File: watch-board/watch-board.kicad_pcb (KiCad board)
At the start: 2 copper layers, 39.2 x 40 mm, 44 parts, among them J1 Conn_01x05_Male, J2 Conn_02x05, J3 FPC-Conn_01x08, U1 MCU_STM32L051K8Tx, U2 Regulator_LTC3531-3, U3 Regulator_BQ25504

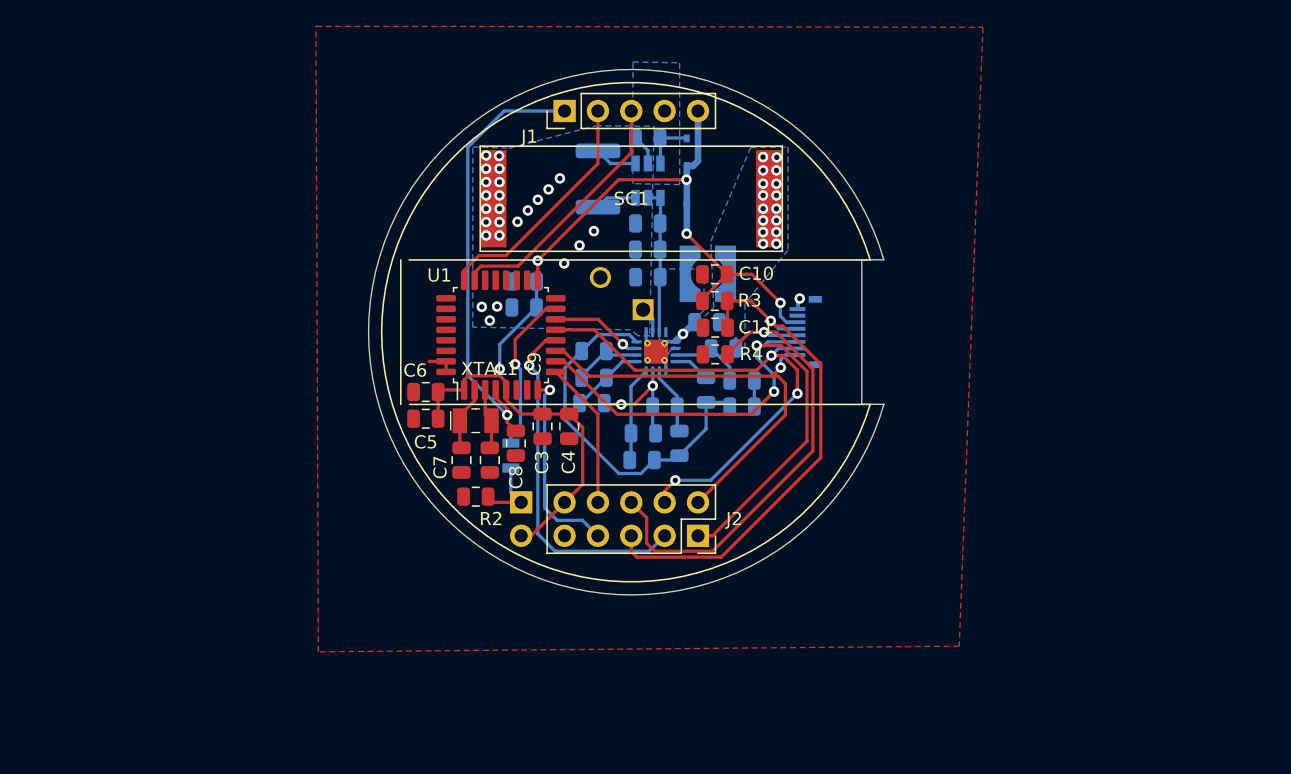
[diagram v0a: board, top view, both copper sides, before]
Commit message: Stopping work on Watch-V2. Changing driver & Display on Watch-V1.
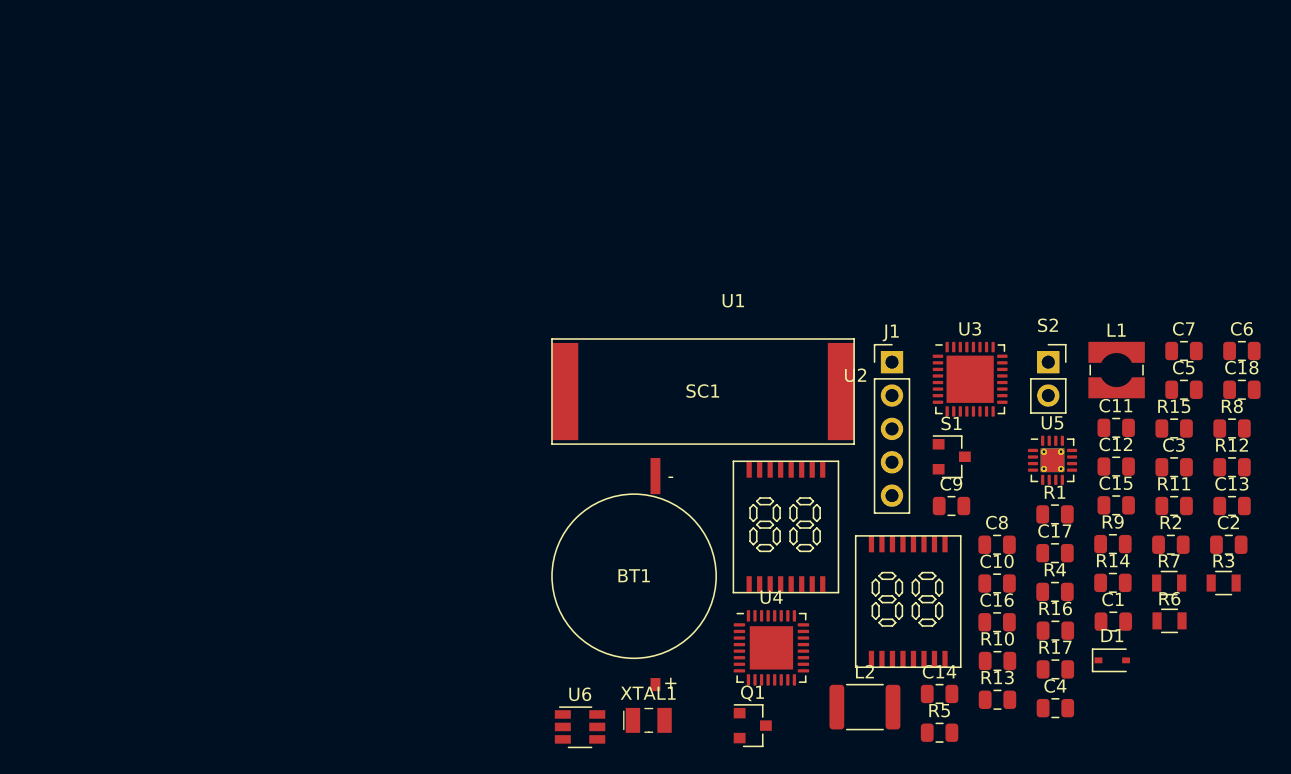
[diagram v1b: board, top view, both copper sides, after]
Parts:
- removed J2: Conn_02x05, Connector_PinSocket_2.54mm:PinSocket_2x05_P2.54mm_Vertical
- removed J3: FPC-Conn_01x08, luke-footprints:Connector_Molex-5014610891
- added C18: C_0.1uF, Capacitor_SMD:C_0805_2012Metric, F.Cu at (186.5, 104.4)
- added Q1: Transistor_MMBT3906, Package_TO_SOT_SMD:SOT-23, F.Cu at (149.2, 130.0)
- added R15: R_6.04M, Resistor_SMD:R_0805_2012Metric, F.Cu at (181.3, 107.3)
- added R16: R_10M, Resistor_SMD:R_0805_2012Metric, F.Cu at (172.3, 122.7)
- added R17: R_3.83M, Resistor_SMD:R_0805_2012Metric, F.Cu at (172.3, 125.7)
- added S2: Switch_1767, Connector_PinSocket_2.54mm:PinSocket_1x02_P2.54mm_Vertical, F.Cu at (171.7, 102.3)
- added U4: MCU_STM32L051K8Ux, Package_DFN_QFN:QFN-32-1EP_5x5mm_P0.5mm_EP3.3x3.3mm, F.Cu at (150.7, 124.0)
- added U5: Regulator_BQ25504, Package_DFN_QFN:VQFN-16-1EP_3x3mm_P0.5mm_EP1.8x1.8mm_ThermalVias, F.Cu at (172.1, 109.8)
- added U6: Regulator_LTC3531-3, Package_TO_SOT_SMD:TSOT-23-6, F.Cu at (136.1, 130.1)
- BT1: footprint Battery:Battery_Panasonic_CR1220-VCN_Vertical_CircularHoles -> luke-footprints:BAT_ML1220-F1A; moved to F.Cu
- C1, C13, C14, C2, D1, R10: moved to F.Cu
- C10: value C_2.2uF -> C_0.1uF
- C12: value C_2.2uF -> C_1uF; moved to F.Cu
- C15: value C_10uF -> C_2.2uF; moved to F.Cu
- C16: value C_4.7uF -> C_10uF; moved to F.Cu
- C17: value C_0.1uF -> C_4.7uF; moved to F.Cu
- L1: value L_10uH -> L_22uH; footprint Inductor_SMD:L_1812_4532Metric -> Inductor_SMD:L_Wuerth_WE-TPC-3816; moved to F.Cu
- L2: value L_22uH -> L_10uH; footprint Inductor_SMD:L_Wuerth_WE-TPC-3816 -> Inductor_SMD:L_1812_4532Metric; moved to F.Cu
- R1: value R_330 -> R_1K; footprint footprints:R_0805_OEM -> Resistor_SMD:R_0805_2012Metric; moved to F.Cu
- R11: value R_5.11M -> R_5.62M; moved to F.Cu
- R12: value R_6.04M -> R_806K; moved to F.Cu
- R13: value R_10M -> R_4.22M; moved to F.Cu
- R14: value R_3.83M -> R_5.11M; moved to F.Cu
- R2: value R_220K -> R_1K
- R3: value R_10K -> R_330; footprint Resistor_SMD:R_0805_2012Metric -> footprints:R_0805_OEM
- R4: value R_10K -> R_220K
- R5: value R_3.74M -> R_1K; moved to F.Cu
- R6: value R_6.19M -> R_330; footprint Resistor_SMD:R_0805_2012Metric -> footprints:R_0805_OEM; moved to F.Cu
- R7: value R_4.22M -> R_330; footprint Resistor_SMD:R_0805_2012Metric -> footprints:R_0805_OEM; moved to F.Cu
- R8: value R_5.62M -> R_3.74M; moved to F.Cu
- R9: value R_806K -> R_6.19M; moved to F.Cu
- S1: value Switch_1767 -> Switch_RR121-1A23-311; footprint Connector_PinSocket_2.54mm:PinSocket_1x02_P2.54mm_Vertical -> Package_TO_SOT_SMD:SOT-23; moved to F.Cu
- U1: value MCU_STM32L051K8Tx -> LCD_OD-204; footprint Package_QFP:LQFP-32_7x7mm_P0.8mm -> luke-footprints:LCD_OD-204
- U2: value Regulator_LTC3531-3 -> LCD_OD-204; footprint Package_TO_SOT_SMD:TSOT-23-6 -> luke-footprints:LCD_OD-204; moved to F.Cu
- U3: value Regulator_BQ25504 -> Display-Driver_PCA8561ANH; footprint Package_DFN_QFN:VQFN-16-1EP_3x3mm_P0.5mm_EP1.8x1.8mm_ThermalVias -> Package_DFN_QFN:QFN-32-1EP_5x5mm_P0.5mm_EP3.6x3.6mm; moved to F.Cu
- moved C6 62.2 mm to (186.5, 101.4)
- moved C5 57.8 mm to (182.1, 104.4)
- moved C2 57.3 mm to (185.5, 116.2)
- moved C7 55.6 mm to (182.1, 101.4), turned to 0 degrees
- moved R2 53.0 mm to (181.1, 116.2), turned to 0 degrees
- moved C1 50.8 mm to (176.7, 122.0)
- moved D1 50.5 mm to (176.6, 125.0), turned to 0 degrees
- moved C3 48.2 mm to (181.3, 110.3), turned to 0 degrees
- moved R11 45.7 mm to (181.3, 113.2), turned to 0 degrees
- moved C15 45.3 mm to (176.9, 113.2), turned to 0 degrees
- moved R8 45.0 mm to (185.7, 107.3)
- moved R3 44.3 mm to (185.1, 119.1)
- moved C4 42.8 mm to (172.3, 128.6), turned to 0 degrees
- moved L1 42.1 mm to (176.9, 102.9), turned to 0 degrees
- moved R1 41.7 mm to (172.3, 113.9), turned to 0 degrees
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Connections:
- C10 pad 1: VDD -> /VDISP
- C10 pad 2: GND -> Net-(C10-Pad2)
- C11 pad 1: /DISP -> /VDISP
- C11 pad 2: GND -> Net-(C11-Pad2)
- C12 pad 1: /LOAD -> VDD
- C15 pad 1: Net-(C15-Pad1) -> /LOAD
- C16 pad 1: /LOAD -> Net-(C16-Pad1)
- D1 pad 2: Net-(C15-Pad1) -> Net-(C16-Pad1)
- L1 pad 1: Net-(L1-Pad1) -> Net-(C14-Pad1)
- L2 pad 1: Net-(C14-Pad1) -> Net-(L2-Pad1)
- R1 pad 1: Net-(R1-Pad1) -> VCC
- R1 pad 2: /BUTTON -> /SDA
- R10 pad 1: /OK_HYST -> Net-(R10-Pad1)
- R10 pad 2: /OK_PROG -> /VBAT_UV
- R11 pad 1: /OK_PROG -> /VBAT_UV
- R12 pad 1: Net-(R12-Pad1) -> Net-(R10-Pad1)
- R12 pad 2: GND -> /OK_HYST
- R13 pad 1: Net-(R13-Pad1) -> /OK_HYST
- R13 pad 2: Net-(R12-Pad1) -> /OK_PROG
- R14 pad 1: Net-(C14-Pad1) -> /OK_PROG
- R14 pad 2: Net-(R13-Pad1) -> GND
- R2 pad 1: Net-(R1-Pad1) -> VCC
- R2 pad 2: GND -> /SCL
- R3 pad 1: VDD -> Net-(R3-Pad1)
- R3 pad 2: /DISP -> /BUTTON
- R4 pad 1: /EXTCOMIN -> Net-(R3-Pad1)
- R5 pad 1: Net-(R5-Pad1) -> VCC
- R5 pad 2: /VBAT_OV -> Net-(Q1-Pad1)
- R6 pad 1: /VBAT_OV -> Net-(R6-Pad1)
- R6 pad 2: GND -> /SWITCH
- R7 pad 1: Net-(R5-Pad1) -> Net-(Q1-Pad1)
- R7 pad 2: /VBAT_UV -> /DISP
- R8 pad 1: /VBAT_UV -> Net-(R10-Pad1)
- R8 pad 2: GND -> /VBAT_OV
- R9 pad 1: Net-(R5-Pad1) -> /VBAT_OV
- R9 pad 2: /OK_HYST -> GND
- S1 pad 1: Net-(R1-Pad1) -> VDD
- S1 pad 2: VDD -> Net-(R6-Pad1)
- U1 pad 1: VDD -> /COM1
- U1 pad 10: /NSS -> /2A
- U1 pad 11: /SCK -> /2B
- U1 pad 12: /MISO -> /2C
- U1 pad 13: /MOSI -> /2D
- U1 pad 14: /VBAT_OK -> /2E
- U1 pad 15: /BUTTON -> /2F
- U1 pad 16: GND -> /2G
- U1 pad 2: Net-(C7-Pad1) -> /1G
- U1 pad 3: Net-(C9-Pad1) -> /1F
- U1 pad 4: /RST -> /1E
- U1 pad 5: VDD -> /1D
- U1 pad 6: Net-(U1-Pad6) -> /1C
- U1 pad 7: Net-(U1-Pad7) -> /1B
- U1 pad 8: /PA2 -> /1A
- U1 pad 9: /PA3 -> Net-(U1-Pad9)
- U2 pad 1: Net-(L1-Pad2) -> /COM2
- U2 pad 2: GND -> /1G
- U2 pad 3: Net-(C15-Pad1) -> /1F
- U2 pad 4: /LOAD -> /1E
- U2 pad 5: /LOAD -> /1D
- U2 pad 6: Net-(L1-Pad1) -> /1C
- U3 pad 1: GND -> /COM2
- U3 pad 10: /OK_PROG -> GND
- U3 pad 11: /VBAT_OK -> GND
- U3 pad 12: GND -> /1G
- U3 pad 13: GND -> /1F
- U3 pad 14: Net-(BT1-Pad1) -> /1E
- U3 pad 15: /LOAD -> /1D
- U3 pad 16: Net-(L2-Pad2) -> /1C
- U3 pad 17: GND -> /1B
- U3 pad 2: Net-(C14-Pad1) -> Net-(C11-Pad2)
- U3 pad 3: Net-(R13-Pad1) -> Net-(C10-Pad2)
- U3 pad 4: Net-(C13-Pad1) -> GND
- U3 pad 5: GND -> /RESET
- U3 pad 6: /VBAT_OV -> GND
- U3 pad 7: Net-(R5-Pad1) -> Net-(U3-Pad7)
- U3 pad 8: /VBAT_UV -> /SCL
- U3 pad 9: /OK_HYST -> /SDA
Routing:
- net VDD: track 76.8 -> 0.00 mm, vias 5 -> 0
- net /NSS: track 46.9 -> 0.00 mm, vias 2 -> 0
- net GND: track 41.6 -> 0.00 mm, vias 27 -> 0
- net /DISP: track 39.2 -> 0.00 mm, vias 1 -> 0
- net /MOSI: track 38.0 -> 0.00 mm, vias 3 -> 0
- net /EXTCOMIN: track 36.4 -> 0.00 mm, vias 1 -> 0
- net /RST: track 34.5 -> 0.00 mm, vias 1 -> 0
- net /SCK: track 32.7 -> 0.00 mm, vias 1 -> 0
- net /MISO: track 27.0 -> 0.00 mm, vias 1 -> 0
- net /SWDIO: track 19.5 -> 0.00 mm
- net /SWCLK: track 18.8 -> 0.00 mm
- net /PA2: track 15.0 -> 0.00 mm, vias 1 -> 0
- net /BUTTON: track 12.4 -> 0.00 mm, vias 1 -> 0
- net /LOAD: track 11.3 -> 0.00 mm
- net /PA3: track 11.3 -> 0.00 mm
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- removed copper zone on B.Cu, net GND
- removed copper zone on F.Cu, net GND
- removed copper zone on B.Cu, net Net-(C14-Pad1)
- removed copper zone on B.Cu, net Net-(L2-Pad2)
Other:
- board outline removed

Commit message: Starting Layout -- updated parts with smaller footprints for better layout
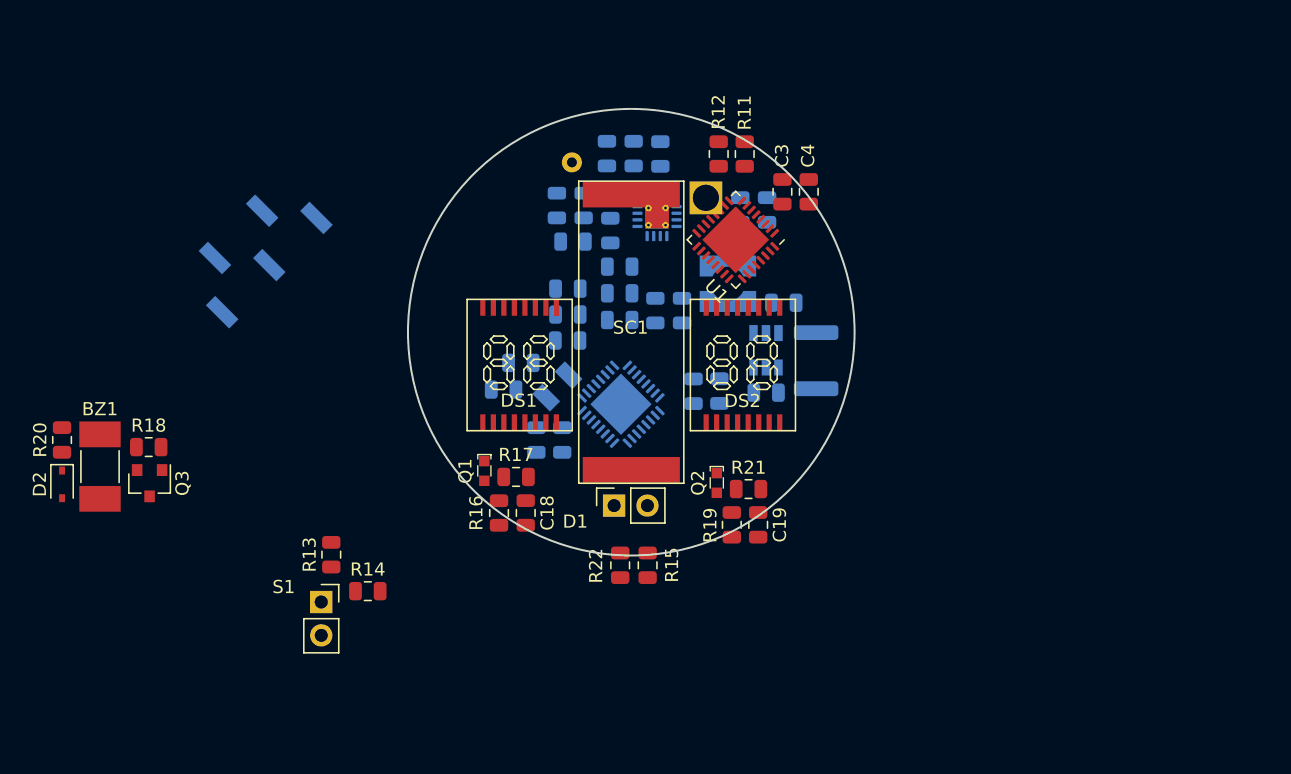
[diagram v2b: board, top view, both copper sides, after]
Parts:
- removed S2: Switch_1767, Connector_PinSocket_2.54mm:PinSocket_1x02_P2.54mm_Vertical
- removed U5: Regulator_BQ25504, Package_DFN_QFN:VQFN-16-1EP_3x3mm_P0.5mm_EP1.8x1.8mm_ThermalVias
- removed U6: Regulator_LTC3531-3, Package_TO_SOT_SMD:TSOT-23-6
- added BZ1: Buzzer_Piezo-35mm, Fuse:Fuse_Littelfuse-NANO2-451_453, F.Cu at (99.6, 110.2)
- added C19: C_100uF, Capacitor_SMD:C_0805_2012Metric, F.Cu at (149.7, 114.7)
- added D2: D-Schotkey_BAT54HT1G, Diode_SMD:D_SOD-323, F.Cu at (96.7, 111.6)
- added DS1: LCD_OD-204, luke-footprints:LCD_OD-204, F.Cu at (127.5, 97.5)
- added DS2: LCD_OD-204, luke-footprints:LCD_OD-204, F.Cu at (144.5, 97.5)
- added Q2: Phototransistor_ALS-PT19-315C, Digikey-footprints:LED_2-SMD_No_Lead_1.7x0.8mm, F.Cu at (146.5, 111.5)
- added Q3: Transistor_MMBT3904-TP, Package_TO_SOT_SMD:SOT-23, F.Cu at (103.3, 111.5)
- added R18: R_10K, Resistor_SMD:R_0805_2012Metric, F.Cu at (103.3, 108.7)
- added R19: R_4.87K, Resistor_SMD:R_0805_2012Metric, F.Cu at (147.7, 114.7)
- added R20: R_160, Resistor_SMD:R_0805_2012Metric, F.Cu at (96.7, 108.2)
- added R21: R_160, Resistor_SMD:R_0805_2012Metric, F.Cu at (148.9, 111.9)
- added R22: R_2.3K, Resistor_SMD:R_0805_2012Metric, F.Cu at (139.2, 117.7)
- BT1: value BAT_ML1220 -> BAT_ML2020-V1A; footprint luke-footprints:BAT_ML1220-F1A -> luke-footprints:Battery_Panasonic-ML-2020-V1A; moved to B.Cu
- C1: value C_0.1uF -> C_0.01uF; moved to B.Cu
- C10, C8, L1, L2, U4, XTAL1: moved to B.Cu
- C11: value C_0.1uF -> C_1uF; moved to B.Cu
- C12: value C_1uF -> C_0.1uF; moved to B.Cu
- C13: value C_0.01uF -> C_10uF; moved to B.Cu
- C14, C17: value C_4.7uF -> C_20pF; moved to B.Cu
- C15: value C_2.2uF -> C_10uF; moved to B.Cu
- C16, C6: value C_10uF -> C_0.1uF; moved to B.Cu
- C18: value C_0.1uF -> C_100uF
- C2: value C_1uF -> C_4.7uF; moved to B.Cu
- C4: value C_1uF -> C_0.1uF
- C5: value C_0.1uF -> C_4.7uF; moved to B.Cu
- C7: value C_20pF -> C_2.2uF; moved to B.Cu
- C9: value C_20pF -> C_1uF; moved to B.Cu
- D1: value D-Schotkey_BAT54HT1G -> LED_WP710A10LSECK-J4; footprint Diode_SMD:D_SOD-323 -> Connector_PinSocket_2.54mm:PinSocket_1x02_P2.54mm_Vertical
- J1: value Conn_01x05_Male -> Conn_01x05_Male_SMD; footprint Connector_PinHeader_2.54mm:PinHeader_1x05_P2.54mm_Vertical -> Connector_PinHeader_2.54mm:PinHeader_1x05_P2.54mm_Vertical_SMD_Pin1Left; moved to B.Cu
- Q1: value Transistor_MMBT3906 -> Phototransistor_ALS-PT19-315C; footprint Package_TO_SOT_SMD:SOT-23 -> Digikey-footprints:LED_2-SMD_No_Lead_1.7x0.8mm
- R1: value R_1K -> R_3.74M; moved to B.Cu
- R10: value R_4.22M -> R_3.83M; moved to B.Cu
- R11: value R_5.62M -> R_4.7K
- R12: value R_806K -> R_4.7K
- R13: value R_4.22M -> R_604
- R14: value R_5.11M -> R_10K
- R15: value R_6.04M -> R_1.5K
- R16: value R_10M -> R_4.87K
- R17: value R_3.83M -> R_160
- R2: value R_1K -> R_6.19M; moved to B.Cu
- R3, R6: value R_330 -> R_4.22M; footprint footprints:R_0805_OEM -> Resistor_SMD:R_0805_2012Metric; moved to B.Cu
- R4: value R_220K -> R_5.62M; moved to B.Cu
- R5: value R_1K -> R_806K; moved to B.Cu
- R7: value R_330 -> R_5.11M; footprint footprints:R_0805_OEM -> Resistor_SMD:R_0805_2012Metric; moved to B.Cu
- R8: value R_3.74M -> R_6.04M; moved to B.Cu
- R9: value R_6.19M -> R_10M; moved to B.Cu
- S1: value Switch_RR121-1A23-311 -> Switch_1767; footprint Package_TO_SOT_SMD:SOT-23 -> Connector_PinSocket_2.54mm:PinSocket_1x02_P2.54mm_Vertical
- U1: value LCD_OD-204 -> Display-Driver_PCA8561ANH; footprint luke-footprints:LCD_OD-204 -> Package_DFN_QFN:QFN-32-1EP_5x5mm_P0.5mm_EP3.6x3.6mm
- U2: value LCD_OD-204 -> Regulator_BQ25504; footprint luke-footprints:LCD_OD-204 -> Package_DFN_QFN:VQFN-16-1EP_3x3mm_P0.5mm_EP1.8x1.8mm_ThermalVias; moved to B.Cu
- U3: value Display-Driver_PCA8561ANH -> Regulator_LTC3531-3; footprint Package_DFN_QFN:QFN-32-1EP_5x5mm_P0.5mm_EP3.6x3.6mm -> Package_TO_SOT_SMD:TSOT-23-6; moved to B.Cu
- moved R14 56.7 mm to (119.9, 119.7)
- moved R3 56.6 mm to (136.4, 90.4), turned to 90 degrees
- moved C18 55.3 mm to (132.0, 113.8), turned to 270 degrees
- moved R6 54.1 mm to (140.2, 86.4), turned to 90 degrees
- moved R13 51.9 mm to (117.2, 116.9), turned to 90 degrees
- moved C13 51.2 mm to (134.7, 108.2), turned to 90 degrees
- moved R2 51.0 mm to (135.6, 93.1), turned to 180 degrees
- moved R5 50.8 mm to (138.1, 86.4), turned to 90 degrees
- moved R7 50.7 mm to (142.2, 86.4), turned to 90 degrees
- moved J1 49.3 mm to (111.3, 93.7), turned to 135 degrees
- moved S1 49.3 mm to (116.4, 120.5)
- moved R4 48.0 mm to (134.3, 90.4), turned to 90 degrees
- moved R8 47.7 mm to (139.1, 97.0), turned to 180 degrees
- moved C1 46.3 mm to (139.1, 95.0), turned to 180 degrees
- moved R12 45.8 mm to (146.7, 86.4), turned to 270 degrees
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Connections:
- C1 pad 1: GND -> Net-(C1-Pad1)
- C1 pad 2: VDD -> GND
- C10 pad 1: /VDISP -> GND
- C10 pad 2: Net-(C10-Pad2) -> VDD
- C11 pad 1: /VDISP -> GND
- C11 pad 2: Net-(C11-Pad2) -> VDD
- C12 pad 1: VDD -> GND
- C12 pad 2: GND -> VDD
- C13 pad 1: Net-(C13-Pad1) -> GND
- C13 pad 2: GND -> VDD
- C15 pad 1: /LOAD -> VDD
- C16 pad 1: Net-(C16-Pad1) -> /RST
- C17 pad 1: /LOAD -> Net-(C17-Pad1)
- C18 pad 1: /LOAD -> /LIGHT_L
- C2 pad 1: GND -> Net-(C2-Pad1)
- C2 pad 2: VDD -> GND
- C3 pad 1: GND -> VDD
- C3 pad 2: VDD -> Net-(C3-Pad2)
- C4 pad 1: GND -> VDD
- C4 pad 2: VDD -> Net-(C4-Pad2)
- C5 pad 1: GND -> /LOAD
- C5 pad 2: VDD -> GND
- C6 pad 1: GND -> /LOAD
- C6 pad 2: VDD -> GND
- C7 pad 1: Net-(C7-Pad1) -> /LOAD
- C8 pad 1: /RST -> GND
- C8 pad 2: GND -> VDD
- C9 pad 1: Net-(C9-Pad1) -> GND
- C9 pad 2: GND -> VDD
- D1 pad 1: VDD -> GND
- D1 pad 2: Net-(C16-Pad1) -> Net-(D1-Pad2)
- L1 pad 1: Net-(C14-Pad1) -> Net-(C2-Pad1)
- Q1 pad 1: Net-(Q1-Pad1) -> /VLIGHT_L
- Q1 pad 2: /VDISP -> Net-(Q1-Pad2)
- R1 pad 1: VCC -> Net-(R1-Pad1)
- R1 pad 2: /SDA -> /VBAT_OV
- R10 pad 1: Net-(R10-Pad1) -> Net-(C2-Pad1)
- R10 pad 2: /VBAT_UV -> Net-(R10-Pad2)
- R11 pad 1: /VBAT_UV -> VCC
- R11 pad 2: GND -> /SDA
- R12 pad 1: Net-(R10-Pad1) -> VCC
- R12 pad 2: /OK_HYST -> /SCL
- R13 pad 1: /OK_HYST -> Net-(R13-Pad1)
- R13 pad 2: /OK_PROG -> /BUTTON
- R14 pad 1: /OK_PROG -> Net-(R13-Pad1)
- R15 pad 1: Net-(R15-Pad1) -> /LIGHT
- R15 pad 2: GND -> Net-(D1-Pad2)
- R16 pad 1: Net-(R16-Pad1) -> Net-(Q1-Pad2)
- R16 pad 2: Net-(R15-Pad1) -> GND
- R17 pad 1: Net-(C14-Pad1) -> /LIGHT_L
- R17 pad 2: Net-(R16-Pad1) -> Net-(Q1-Pad2)
- R2 pad 1: VCC -> /VBAT_OV
- R2 pad 2: /SCL -> GND
- R3 pad 1: Net-(R3-Pad1) -> Net-(R1-Pad1)
- R3 pad 2: /BUTTON -> /VBAT_UV
- R4 pad 1: Net-(R3-Pad1) -> /VBAT_UV
- R5 pad 1: VCC -> Net-(R1-Pad1)
- R5 pad 2: Net-(Q1-Pad1) -> /OK_HYST
- R6 pad 1: Net-(R6-Pad1) -> /OK_HYST
- R6 pad 2: /SWITCH -> /OK_PROG
- R7 pad 1: Net-(Q1-Pad1) -> /OK_PROG
- R7 pad 2: /DISP -> GND
- R8 pad 1: Net-(R10-Pad1) -> Net-(R8-Pad1)
- R8 pad 2: /VBAT_OV -> GND
- R9 pad 1: /VBAT_OV -> Net-(R10-Pad2)
- R9 pad 2: GND -> Net-(R8-Pad1)
- S1 pad 1: VDD -> Net-(R13-Pad1)
- S1 pad 2: Net-(R6-Pad1) -> VDD
- SC1 pad 1: Net-(C14-Pad1) -> Net-(C2-Pad1)
- U1 pad 1: /COM1 -> /COM2
- U1 pad 10: /2A -> GND
- U1 pad 11: /2B -> GND
- U1 pad 12: /2C -> /1G
- U1 pad 13: /2D -> /1F
- U1 pad 14: /2E -> /1E
- U1 pad 15: /2F -> /1D
- U1 pad 16: /2G -> /1C
- U1 pad 2: /1G -> Net-(C4-Pad2)
- U1 pad 3: /1F -> Net-(C3-Pad2)
- U1 pad 4: /1E -> GND
- U1 pad 5: /1D -> /RESET
- U1 pad 6: /1C -> GND
- U1 pad 7: /1B -> Net-(U1-Pad7)
- U1 pad 8: /1A -> /SCL
- U1 pad 9: Net-(U1-Pad9) -> /SDA
- U2 pad 1: /COM2 -> GND
- U2 pad 10: /2A -> /OK_PROG
- U2 pad 11: /2B -> /VBAT_OK
- U2 pad 12: /2C -> GND
- U2 pad 13: /2D -> GND
- U2 pad 14: /2E -> Net-(BT1-PadPos)
- U2 pad 15: /2F -> /LOAD
- U2 pad 16: /2G -> Net-(L1-Pad2)
- U2 pad 2: /1G -> Net-(C2-Pad1)
- U2 pad 3: /1F -> Net-(R10-Pad2)
- U2 pad 4: /1E -> Net-(C1-Pad1)
- U2 pad 5: /1D -> GND
- U2 pad 6: /1C -> /VBAT_OV
- U2 pad 7: /1B -> Net-(R1-Pad1)
- U2 pad 8: /1A -> /VBAT_UV
- U2 pad 9: Net-(U2-Pad9) -> /OK_HYST
- U3 pad 1: /COM2 -> Net-(L2-Pad2)
- U3 pad 2: Net-(C11-Pad2) -> GND
- U3 pad 3: Net-(C10-Pad2) -> VDD
- U3 pad 4: GND -> /LOAD
- U3 pad 5: /RESET -> /LOAD
- U3 pad 6: GND -> Net-(L2-Pad1)
- U4 pad 10: Net-(U4-Pad10) -> /VBAT_OK
- U4 pad 11: Net-(U4-Pad11) -> /VLIGHT_L
- U4 pad 12: Net-(U4-Pad12) -> /VLIGHT_R
- U4 pad 13: Net-(U4-Pad13) -> /LIGHT
- U4 pad 18: Net-(U4-Pad18) -> /RESET
- U4 pad 2: Net-(C7-Pad1) -> Net-(C14-Pad1)
- U4 pad 20: /SWITCH -> Net-(U4-Pad20)
- U4 pad 3: Net-(C9-Pad1) -> Net-(C17-Pad1)
- U4 pad 6: /VBAT_OK -> /BUZZER
- U4 pad 8: /RESET -> /LIGHT_L
- U4 pad 9: /DISP -> /LIGHT_R
- XTAL1 pad 1: Net-(C7-Pad1) -> Net-(C14-Pad1)
- XTAL1 pad 2: Net-(C9-Pad1) -> Net-(C17-Pad1)
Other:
- board outline added: 34 x 34 mm

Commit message: Layout (Rev 1) Complete
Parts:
- added J2: Conn_PAD, luke-footprints:Connector_PAD_1mm_Circ, B.Cu at (124.8, 106.7)
- added J3: Conn_PAD, luke-footprints:Connector_PAD_1mm_Circ, B.Cu at (126.0, 108.7)
- added J4: Conn_PAD, luke-footprints:Connector_PAD_1mm_Circ, B.Cu at (129.2, 112.3)
- added J5: Conn_PAD, luke-footprints:Connector_PAD_1mm_Circ, B.Cu at (127.5, 110.5)
- BZ1, C18, C19, C3, C4, D2, Q3, R11, R12, R13, R14, R15, R18, R19, R20, R21, R22: moved to B.Cu
- J1: value Conn_01x05_Male_SMD -> Conn_PAD; footprint Connector_PinHeader_2.54mm:PinHeader_1x05_P2.54mm_Vertical_SMD_Pin1Left -> luke-footprints:Connector_PAD_1mm_Circ
- moved D2 47.5 mm to (143.8, 106.0)
- moved R20 47.5 mm to (143.8, 102.6)
- moved BZ1 41.7 mm to (140.9, 104.6)
- moved R18 34.4 mm to (137.2, 103.1), turned to 0 degrees
- moved Q3 34.3 mm to (137.1, 105.9)
- moved S1 30.5 mm to (145.6, 111.9), turned to 180 degrees
- moved R13 26.8 mm to (143.1, 110.2)
- moved R14 24.2 mm to (143.4, 113.8), turned to 270 degrees
- moved J1 22.6 mm to (132.5, 101.4), turned to 0 degrees
- moved C4 21.4 mm to (132.2, 87.5)
- moved R11 20.9 mm to (128.6, 92.3), turned to 180 degrees
- moved C3 20.3 mm to (131.3, 91.1), turned to 90 degrees
- moved R12 18.5 mm to (128.6, 90.3), turned to 180 degrees
- moved U1 16.6 mm to (131.4, 93.2), turned to 315 degrees
- moved C9 15.4 mm to (132.2, 109.6), turned to 180 degrees
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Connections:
- R11 pad 1: VCC -> VDD
- R12 pad 1: VCC -> VDD
- R20 pad 1: VCC -> VDD
